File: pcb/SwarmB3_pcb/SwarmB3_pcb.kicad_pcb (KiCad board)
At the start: 2 copper layers, 81.8 x 72.1 mm, 52 parts, among them J1 5v_3Pi, J10 ItsyBitsyRight, J11 ItsyBitsyLeft, J2 GND_3Pi, J3 I2C_3V3_Exp, J4 Conn_02x15_M5Stack_Core2, J5 I2C_3Pi, J6 3PI_SWTCH, J8 ProxA, J9 ProxB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

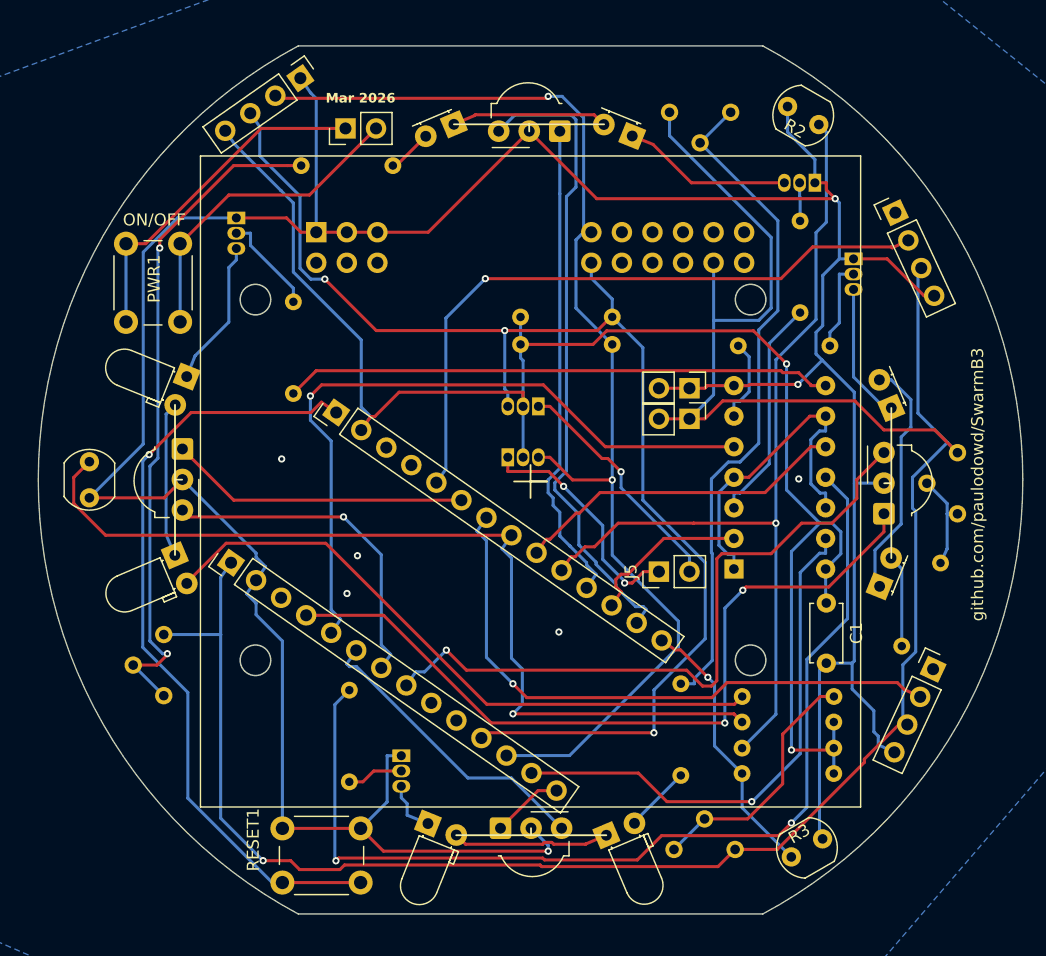
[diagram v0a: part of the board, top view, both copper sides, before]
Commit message: Found errors with the PCB, fixed.  Pin 7 was labelled wrong, so it wasn't connected to the 74HC08.  3 of the pots were located in illogical places, not next to the associated LEDs.  The 74HC08 was also in it's own isolated ground network, but after fixing the other stuff, the new routing fixed the issue.
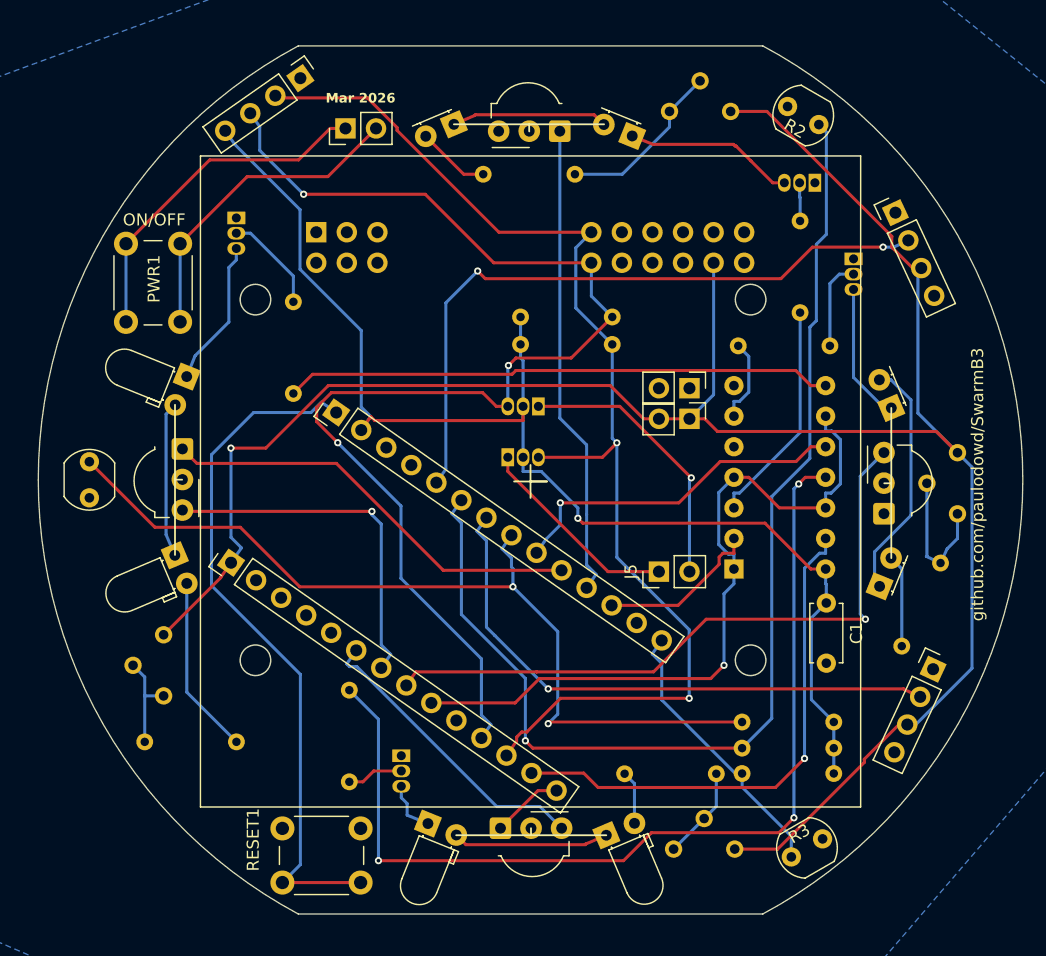
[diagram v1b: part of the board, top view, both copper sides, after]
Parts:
- moved VR4_A1 64.2 mm to (130.4, 63.6), turned to 90 degrees
- moved VR_1A1 61.4 mm to (130.8, 124.9), turned to 90 degrees
- moved VR2_A1 44.3 mm to (88.4, 112.2), turned to 180 degrees
- moved R1 42.2 mm to (94.4, 116.0), turned to 180 degrees
- moved R9 7.54 mm to (114.9, 68.8), turned to 0 degrees
- moved R13 4.67 mm to (126.7, 118.7), turned to 0 degrees
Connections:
- net 21/PA12 renamed 21/PA12/SDA
- net 22/PA13 renamed 22/PA13/SCL
- net 24/PA01 renamed 24/PA01/SCK
- net 25/PA00 renamed 25/PA00/MOSI
- J10 pad 4: 13/PA23 -> 13/PA22
- J11 pad 13: 23/PB23 -> 23/PB23/MISO
- R2 pad 1: A5/19/PA06 -> A1/15/PA05
- R4 pad 2: A5/19/PA06 -> A1/15/PA05
- U1 pad 1: CLK_58K -> 7/PA18
- U1 pad 12: CLK_58K -> 7/PA18
- U1 pad 4: CLK_58K -> 7/PA18
- U1 pad 5: 12/PA23 -> 12/PA22
- U1 pad 9: CLK_58K -> 7/PA18
- UD_2 pad 1: A1/15/PA05 -> A5/19/PA06
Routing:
- net GND: track 279.1 -> 0.00 mm, vias 8 -> 0
- net A1/15/PA05: track 24.9 -> 96.0 mm, vias 0 -> 1
- net 13/PA23: track 65.4 -> 0.00 mm, vias 2 -> 0
- net 7/PA18: track 0.00 -> 60.8 mm, vias 0 -> 1
- net 12/PA23: track 58.7 -> 0.00 mm, vias 1 -> 0
- net 23/PB23: track 53.5 -> 0.00 mm
- net Net-(VR_1A1-CCW): track 55.8 -> 7.73 mm
- net Net-(VR4_A1-CCW): track 56.8 -> 14.4 mm, vias 2 -> 0
- net A5/19/PA06: track 74.5 -> 35.7 mm, vias 1 -> 0
- net Net-(D2_B1-A): track 53.4 -> 14.9 mm
- net CLK_58K: track 27.9 -> 0.00 mm
- net 3V3: track 132.1 -> 105.6 mm, vias 2 -> 1
- net 5V: track 198.5 -> 180.1 mm
- net Net-(VR2_A1-CCW): track 21.0 -> 8.33 mm
- net RST: track 65.2 -> 58.2 mm, vias 1 -> 0
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
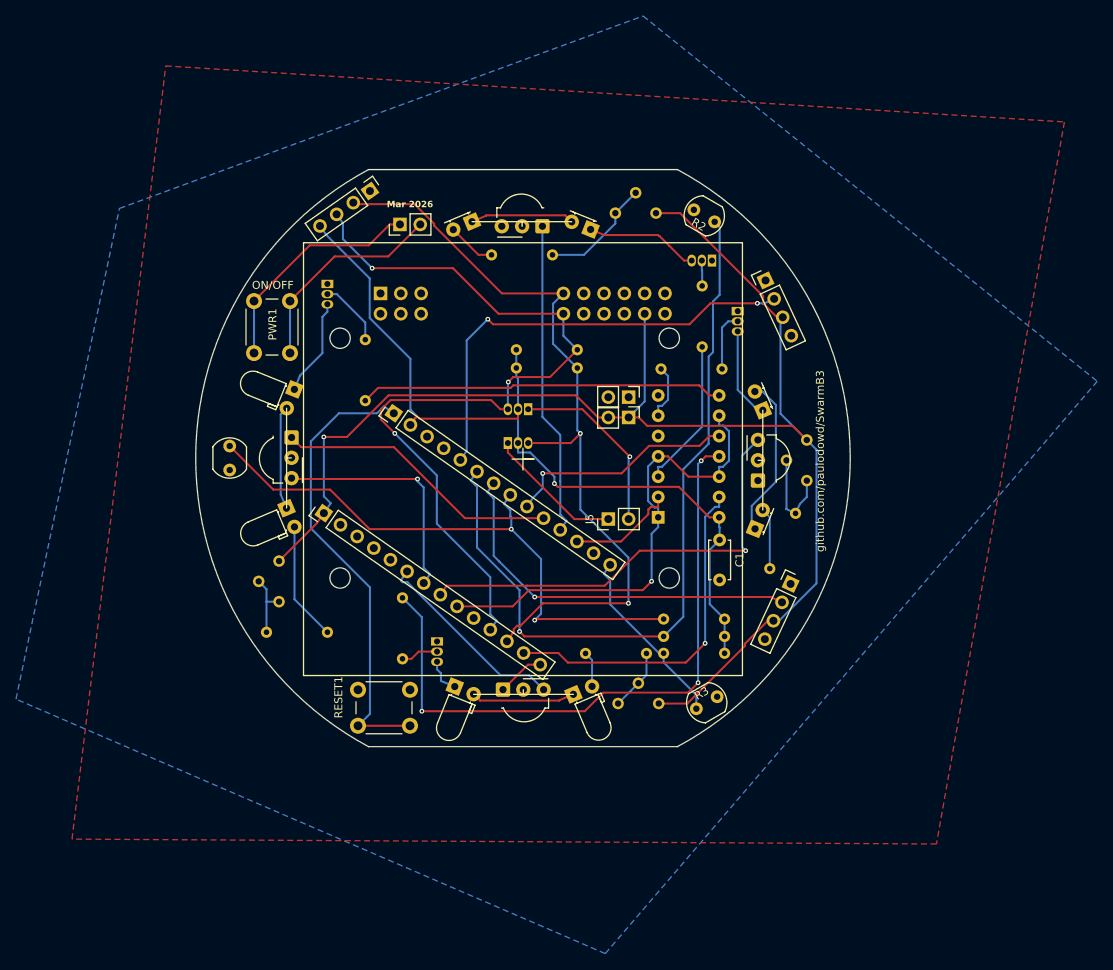
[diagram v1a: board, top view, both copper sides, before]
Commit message: Somehow, I had the pcb manufactured with A1 as rx for a UART, but my latest design files were for A5.  Since I've debugged and tested the PCB as working, I've modified the design files back to using A1.
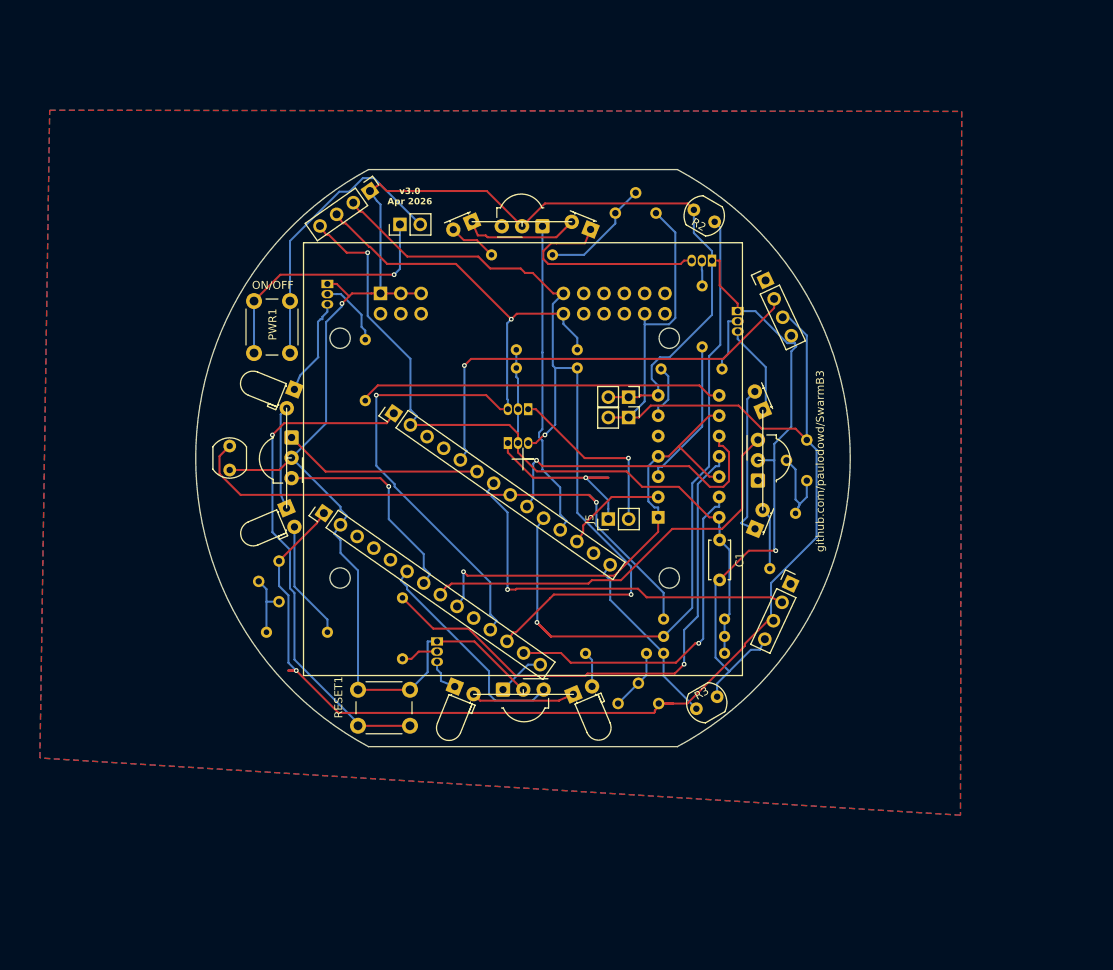
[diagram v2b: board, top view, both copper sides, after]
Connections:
- R2 pad 1: A1/15/PA05 -> A5/19/PA06
- R4 pad 2: A1/15/PA05 -> A5/19/PA06
- UD_2 pad 1: A5/19/PA06 -> A1/15/PA05
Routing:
- net GND: track 0.00 -> 276.3 mm, vias 0 -> 2
- net A1/15/PA05: track 96.0 -> 24.9 mm, vias 1 -> 0
- net A5/19/PA06: track 35.7 -> 94.8 mm, vias 0 -> 1
- net 5V: track 180.1 -> 197.3 mm
- net Net-(R15-Pad1): track 81.6 -> 67.9 mm, vias 3 -> 1
- net Net-(D4_A1-K): track 14.1 -> 27.5 mm
- net SDA_5V: track 17.2 -> 29.8 mm, vias 0 -> 1
- net A4/18/PA04: track 28.9 -> 38.3 mm
- net Net-(J6-Pad2): track 26.7 -> 35.9 mm
- net 21/PA12/SDA: track 98.8 -> 104.4 mm
- net RST: track 58.2 -> 63.7 mm, vias 0 -> 1
- net 9/PA19: track 55.4 -> 51.7 mm, vias 1 -> 0
- net Net-(J6-Pad1): track 28.7 -> 32.0 mm, vias 0 -> 1
- net 11/PA21: track 24.9 -> 27.9 mm
- net 10/PA20: track 29.7 -> 27.0 mm
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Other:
- board text added: "v3.0 Apr 2026"
- board text removed: "Mar 2026"

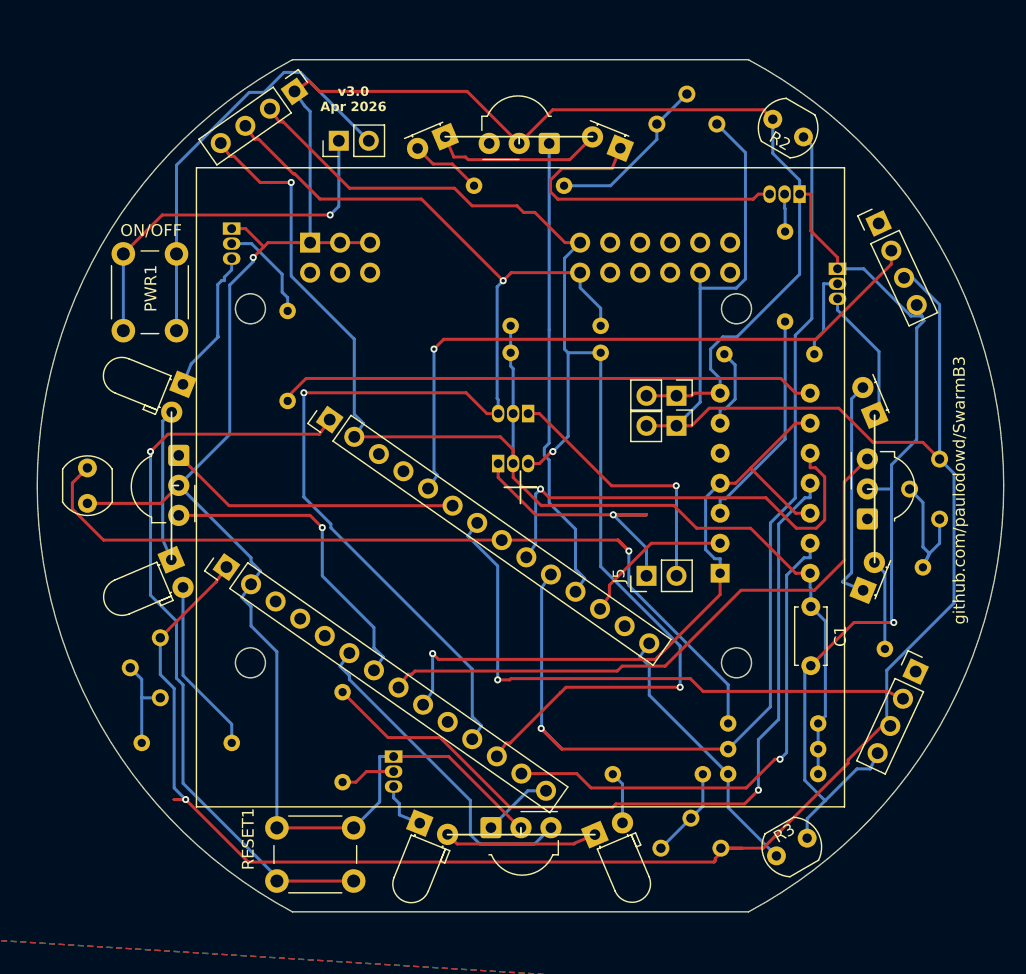
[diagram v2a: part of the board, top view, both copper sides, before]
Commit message: Lots and lots of debugging between hardware and software.  The pcb design worked on the assumption that the UART tx could be inverted in software, as stated in the SAMD51 datasheet.  However, it doesn't work as I expected.  It seems to invert the data, but the idle state remains high.  This causes issues for IR communication because I don't want to saturate the environment with the carrier wave whilst communication is not occuring. I tried a software fix, pulling the gpio low between transmissions.  However, I can't seem to restore the GPIO properly without messing up the protocol overall. I got as far as seeing the bit pattern shifted by 1 bit, which is occuring because the receiver is mis-registering the start bit.  When I look at both sides of the communication on the oscilloscope, I can see that for a batch send (like 10 bytes), the first byte is dropping the start bit.  I haven't been able to get to the bottom of why.  If I do not invert the tx, the problem goes away, but I don't want a non-inverted signal (saturation problem).  I tried some other logic gates.  Surprisingly, 74hc32 (OR) works as a drop in - however, it does mean that for data logic 1, the data stream is actually an on/off pulse train - which is not ideal.  The receiver seems quite robust to this, the datasheet has measures for this sort of thing.  However, I don't want a board that could cause communication defects alongside from what I am investigating in research.  A possible fix is to implement active low LED drivers, which would necessitate an extra transister per UART (e.g. +4).  I don't fancy soldering that, so instead I've updated the pcb to pass tx outputs through a 74hc14 first.  I've tested this on breadboard and it works fine.  It means I can just use the UART interfaces normally without any software SAMD51 inversion.  The current code (ItsyBitsy_test) is a mess from all my debugging chopping and changes.  I'll refactor after testing the new pcb when it arrives.
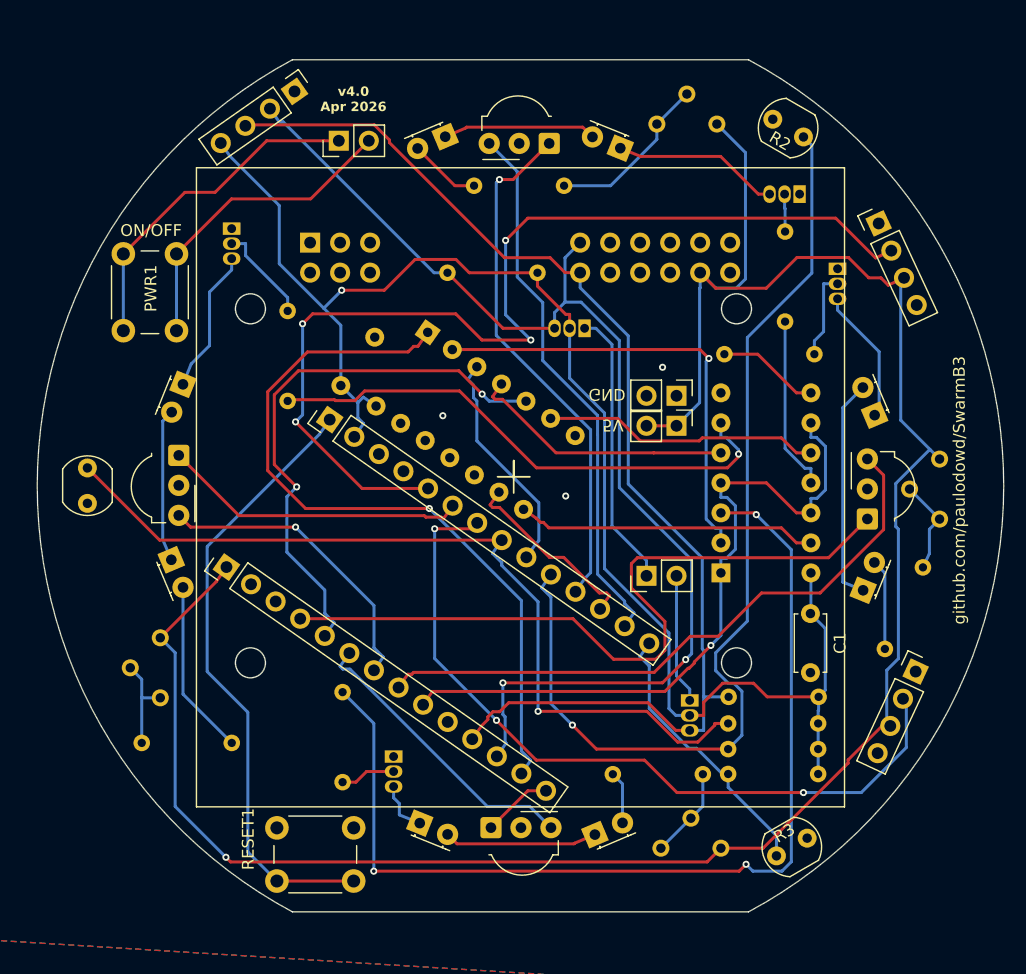
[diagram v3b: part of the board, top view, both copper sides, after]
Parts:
- added C2: 0.1uF, Capacitor_THT:C_Disc_D4.7mm_W2.5mm_P5.00mm, B.Cu at (103.7, 85.7)
- added U2: 74LS08, Package_DIP:DIP-14_W7.62mm_Socket, B.Cu at (135.8, 101.6)
- U1: value 74LS08 -> 74HC14
- moved R20 33.2 mm to (136.5, 112.1), turned to 0 degrees
- moved U1 32.1 mm to (111.0, 81.2), turned to -125 degrees
- moved Q7 27.9 mm to (133.2, 112.4), turned to -90 degrees
- moved R19 14.6 mm to (112.7, 76.2), turned to 0 degrees
- moved Q8 13.6 mm to (124.3, 80.9), turned to 180 degrees
- moved C1 0.59 mm to (143.4, 105.0)
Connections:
- U1 pad 1: 7/PA18 -> 1/PA17
- U1 pad 10: A4/18/PA04 -> unconnected-(U1-Pad10)
- U1 pad 11: Net-(R15-Pad1) -> GND
- U1 pad 12: 7/PA18 -> unconnected-(U1-Pad12)
- U1 pad 13: 1/PA17 -> GND
- U1 pad 2: 25/PA00/MOSI -> Net-(U1-Pad2)
- U1 pad 3: Net-(R18-Pad1) -> A4/18/PA04
- U1 pad 4: 7/PA18 -> Net-(U1-Pad4)
- U1 pad 5: 12/PA22 -> 12/PA23
- U1 pad 6: Net-(R17-Pad1) -> Net-(U1-Pad6)
- U1 pad 8: Net-(R16-Pad1) -> Net-(U1-Pad8)
- U1 pad 9: 7/PA18 -> 25/PA00/MOSI
- UD_3 pad 1: 13/PA23 -> 13/PA22
- UD_4 pad 3: 23/PB23 -> 23/PB23/MISO
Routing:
- net GND: track 276.3 -> 0.00 mm, vias 2 -> 3
- net 13/PA22: track 0.00 -> 62.7 mm
- net 12/PA23: track 0.00 -> 46.7 mm, vias 0 -> 2
- net 23/PB23/MISO: track 0.00 -> 46.2 mm
- net Net-(U1-Pad2): track 0.00 -> 38.5 mm, vias 0 -> 1
- net A0/14/PA02: track 55.0 -> 87.0 mm, vias 1 -> 4
- net Net-(U1-Pad8): track 0.00 -> 25.4 mm
- net Net-(U1-Pad6): track 0.00 -> 23.5 mm
- net Net-(U1-Pad4): track 0.00 -> 22.6 mm
- net 3V3: track 106.1 -> 127.0 mm
- net 1/PA17: track 43.0 -> 63.7 mm
- net A4/18/PA04: track 38.3 -> 19.2 mm, vias 1 -> 0
- net Net-(R15-Pad1): track 67.9 -> 86.1 mm, vias 1 -> 3
- net A2/16/PB08: track 49.5 -> 65.2 mm, vias 1 -> 3
- net Net-(D4_A1-K): track 27.5 -> 14.1 mm
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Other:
- board text added: "5V"
- board text added: "v4.0 Apr 2026"
- board text removed: "+"
- board text removed: "-"
- board text removed: "v3.0 Apr 2026"
